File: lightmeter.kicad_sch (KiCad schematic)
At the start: 41 parts, among them J1 5V input, J2 programmer, J4 VEML7700, J6 OLED Display, J7 Solanoid, Q1 FDV305N, SW1 Shutter, SW2 Value Rot, SW3 BOOT, SW4 Setting Rot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

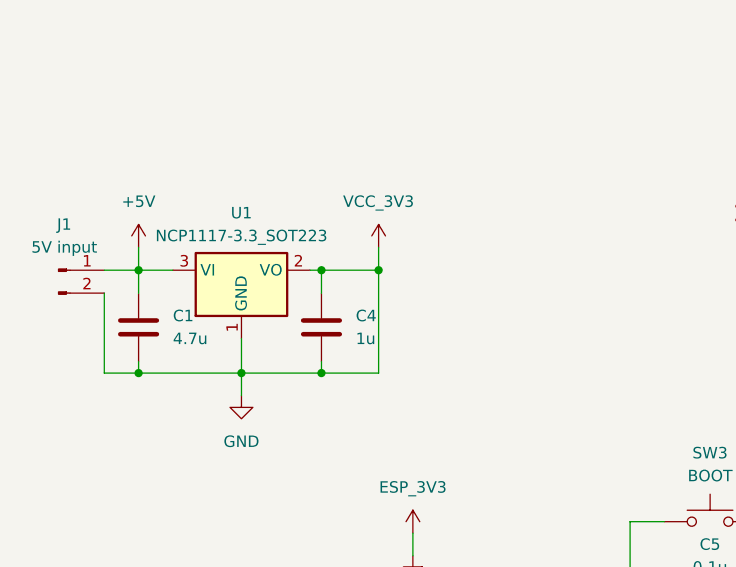
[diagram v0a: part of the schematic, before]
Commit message: ixed even more issues with the footprints, configured placement and ran autorouter. Still have settings to adjust though.
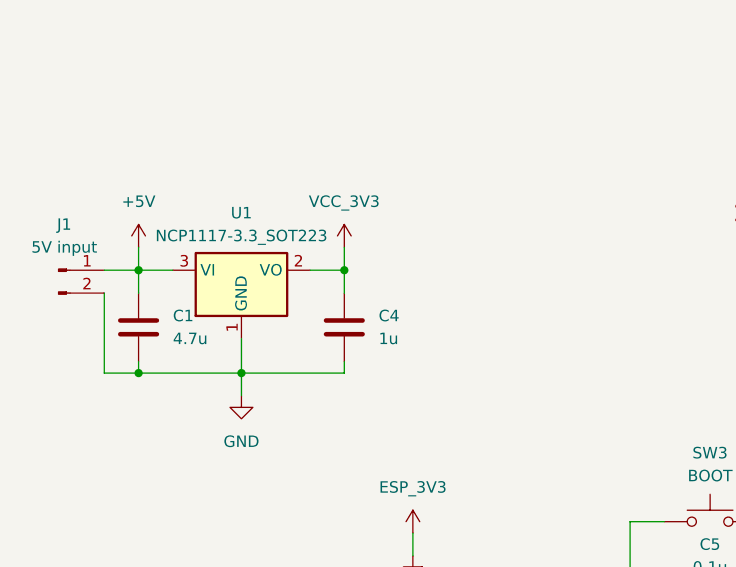
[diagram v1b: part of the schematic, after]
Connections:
- net GND: no longer C10.1, C4.1, C6.1, R10.1, U1.2 (VO)
- new net VCC_3V3: C10.1, C4.1, C6.1, R10.1, U1.2 (VO)
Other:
- moved on the sheet: C4
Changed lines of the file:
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@@
 	)
 	(junction
-		(at 45.72 88.9)
+		(at 48.26 88.9)
 		(diameter 0)
 		(color 0 0 0 0)
@@
 	)
 	(junction
-		(at 52.07 88.9)
-		(diameter 0)
-		(color 0 0 0 0)
-	)
-	(junction
 		(at 36.83 100.33)
 		(diameter 0)
@@
 	)
 	(junction
-		(at 45.72 100.33)
-		(diameter 0)
-		(color 0 0 0 0)
-	)
-	(junction
 		(at 43.18 176.53)
 		(diameter 0)
@@
 	(wire
 		(pts
-			(xy 52.07 86.36) (xy 52.07 88.9)
+			(xy 48.26 86.36) (xy 48.26 88.9)
 		)
 		(stroke
@@
 	(wire
 		(pts
-			(xy 45.72 100.33) (xy 52.07 100.33)
-		)
-		(stroke
-			(width 0)
-			(type default)
-		)
-	)
-	(wire
-		(pts
 			(xy 54.61 158.75) (xy 54.61 161.29)
 		)
@@
 	(wire
 		(pts
-			(xy 52.07 88.9) (xy 45.72 88.9)
-		)
-		(stroke
-			(width 0)
-			(type default)
-		)
-	)
-	(wire
-		(pts
 			(xy 137.16 171.45) (xy 140.97 171.45)
 		)
@@
 	(wire
 		(pts
-			(xy 45.72 88.9) (xy 44.45 88.9)
-		)
-		(stroke
-			(width 0)
-			(type default)
-		)
-	)
-	(wire
-		(pts
 			(xy 166.37 62.23) (xy 172.72 62.23)
 		)
@@
 	(wire
 		(pts
-			(xy 36.83 100.33) (xy 45.72 100.33)
+			(xy 36.83 100.33) (xy 48.26 100.33)
 		)
 		(stroke
@@
 	(wire
 		(pts
-			(xy 45.72 99.06) (xy 45.72 100.33)
+			(xy 48.26 99.06) (xy 48.26 100.33)
 		)
 		(stroke
@@
 	(wire
 		(pts
-			(xy 52.07 100.33) (xy 52.07 88.9)
-		)
-		(stroke
-			(width 0)
-			(type default)
-		)
-	)
-	(wire
-		(pts
 			(xy 54.61 168.91) (xy 54.61 171.45)
 		)
@@
 	(wire
 		(pts
-			(xy 45.72 88.9) (xy 45.72 91.44)
+			(xy 48.26 88.9) (xy 48.26 91.44)
 		)
 		(stroke
@@
 	(wire
 		(pts
+			(xy 44.45 88.9) (xy 48.26 88.9)
+		)
+		(stroke
+			(width 0)
+			(type default)
+		)
+	)
+	(wire
+		(pts
 			(xy 212.09 130.81) (xy 223.52 130.81)
 		)
@@
 	)
 	(symbol
-		(lib_id "boost_converter_module:boost_converter_module")
-		(at 213.36 76.2 0)
-		(unit 1)
-		(exclude_from_sim no)
-		(in_bom yes)
-		(on_board yes)
-		(dnp no)
-		(fields_autoplaced yes)
-		(property "Reference" "U4"
-			(at 220.3462 64.77 0)
-			(effects
-				(font
-					(size 1.27 1.27)
-				)
-			)
-		)
-		(property "Value" "~"
-			(at 220.3462 67.31 0)
-			(effects
-				(font
-					(size 1.27 1.27)
-				)
-			)
-		)
-		(property "Footprint" "Boost_Converter_Module_Footprint:Boost_Converter_Module"
-			(at 213.36 76.2 0)
-			(effects
-				(font
-					(size 1.27 1.27)
-				)
-				(hide yes)
-			)
-		)
-		(property "Datasheet" ""
-			(at 213.36 76.2 0)
-			(effects
-				(font
-					(size 1.27 1.27)
-				)
-				(hide yes)
-			)
-		)
-		(property "Description" ""
-			(at 213.36 76.2 0)
-			(effects
-				(font
-					(size 1.27 1.27)
-				)
-				(hide yes)
-			)
-		)
-		(pin "1"
-		)
-		(pin "3"
-		)
-		(pin "2"
-		)
-		(instances
-			(project ""
-				(path "/d6ab05e9-ebb1-480e-b763-4bcbf117a171"
-					(reference "U4")
-					(unit 1)
-				)
-			)
-		)
-	)
-	(symbol
 		(lib_id "power:+5V")
 		(at 232.41 71.12 0)
@@
 	(symbol
 		(lib_id "power:VCC")
-		(at 52.07 86.36 0)
+		(at 48.26 86.36 0)
 		(unit 1)
 		(exclude_from_sim no)
@@
 		(fields_autoplaced yes)
 		(property "Reference" "#PWR08"
-			(at 52.07 90.17 0)
+			(at 48.26 90.17 0)
 			(effects
 				(font
@@
 		)
 		(property "Value" "VCC_3V3"
-			(at 52.07 81.28 0)
+			(at 48.26 81.28 0)
 			(effects
 				(font
@@
 		)
 		(property "Footprint" ""
-			(at 52.07 86.36 0)
+			(at 48.26 86.36 0)
 			(effects
 				(font
@@
 		)
 		(property "Datasheet" ""
-			(at 52.07 86.36 0)
+			(at 48.26 86.36 0)
 			(effects
 				(font
@@
 		)
 		(property "Description" "Power symbol creates a global label with name \"VCC\""
-			(at 52.07 86.36 0)
+			(at 48.26 86.36 0)
 			(effects
 				(font
@@
 	(symbol
 		(lib_id "Device:C")
-		(at 45.72 95.25 0)
+		(at 48.26 95.25 0)
 		(unit 1)
 		(exclude_from_sim no)
@@
 		(fields_autoplaced yes)
 		(property "Reference" "C4"
-			(at 49.53 93.9799 0)
+			(at 52.07 93.9799 0)
 			(effects
 				(font
@@
 		)
 		(property "Value" "1u"
-			(at 49.53 96.5199 0)
+			(at 52.07 96.5199 0)
 			(effects
 				(font
@@
 		)
 		(property "Footprint" "Capacitor_SMD:C_0805_2012Metric"
-			(at 46.6852 99.06 0)
+			(at 49.2252 99.06 0)
 			(effects
 				(font
@@
 		)
 		(property "Datasheet" "~"
-			(at 45.72 95.25 0)
+			(at 48.26 95.25 0)
 			(effects
 				(font
@@
 		)
 		(property "Description" "Unpolarized capacitor"
-			(at 45.72 95.25 0)
+			(at 48.26 95.25 0)
 			(effects
 				(font
@@
 					(unit 1)
 				)
+			)
+		)
+	)
+	(symbol
+		(lib_id "boost_converter_module:boost_converter_module")
+		(at 213.36 76.2 0)
+		(unit 1)
+		(exclude_from_sim no)
+		(in_bom yes)
+		(on_board yes)
+		(dnp no)
+		(fields_autoplaced yes)
+		(property "Reference" "U4"
+			(at 220.3462 64.77 0)
+			(effects
+				(font
+					(size 1.27 1.27)
+				)
+			)
+		)
+		(property "Value" "~"
+			(at 220.3462 67.31 0)
+			(effects
+				(font
+					(size 1.27 1.27)
+				)
+			)
+		)
+		(property "Footprint" "Boost_Converter_Module_Footprint:Boost_Converter_Module"
+			(at 213.36 76.2 0)
+			(effects
+				(font
+					(size 1.27 1.27)
+				)
+				(hide yes)
+			)
+		)
+		(property "Datasheet" ""
+			(at 213.36 76.2 0)
+			(effects
+				(font
+					(size 1.27 1.27)
+				)
+				(hide yes)
+			)
+		)
+		(property "Description" ""
+			(at 213.36 76.2 0)
+			(effects
+				(font
+					(size 1.27 1.27)
+				)
+				(hide yes)
+			)
+		)
+		(pin "3"
+		)
+		(pin "2"
+		)
+		(pin "1"
+		)
+		(instances
+			(project ""
+				(path "/d6ab05e9-ebb1-480e-b763-4bcbf117a171"
+					(reference "U4")
+					(unit 1)
+				)
